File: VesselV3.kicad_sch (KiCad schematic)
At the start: 370 parts, among them IC1 USB3320C-EZK-TR, IC2 ORDiode(SWD/RST_SWITCH), J1 JTAG/SWD 10pins Headers, U1 LogicLevelShifter, Y1 25MHz

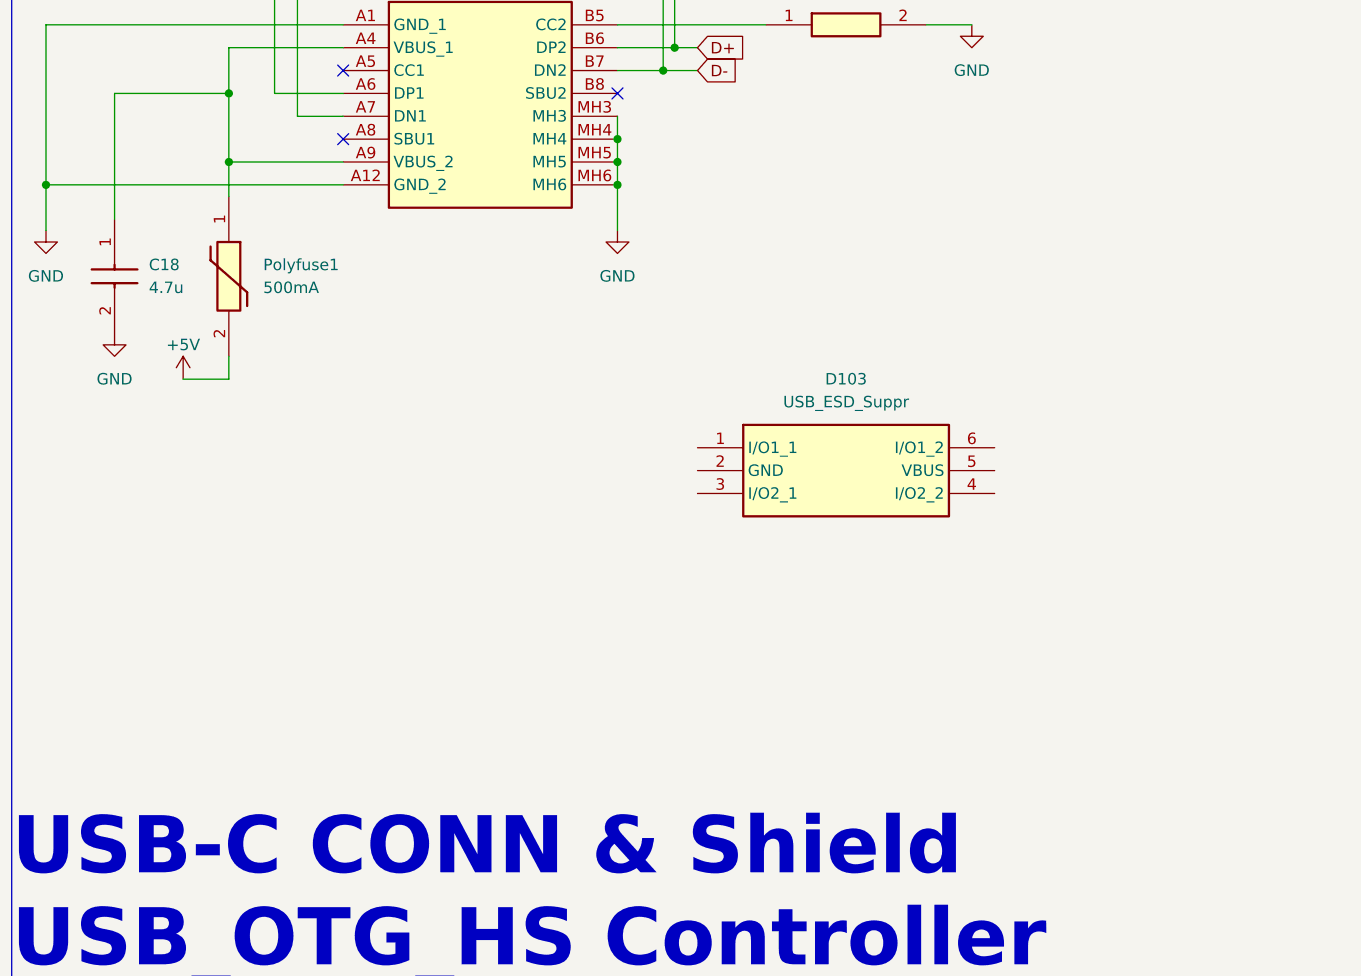
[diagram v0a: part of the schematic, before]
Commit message: ESD & Reverse Pol protections / + 5V regulator
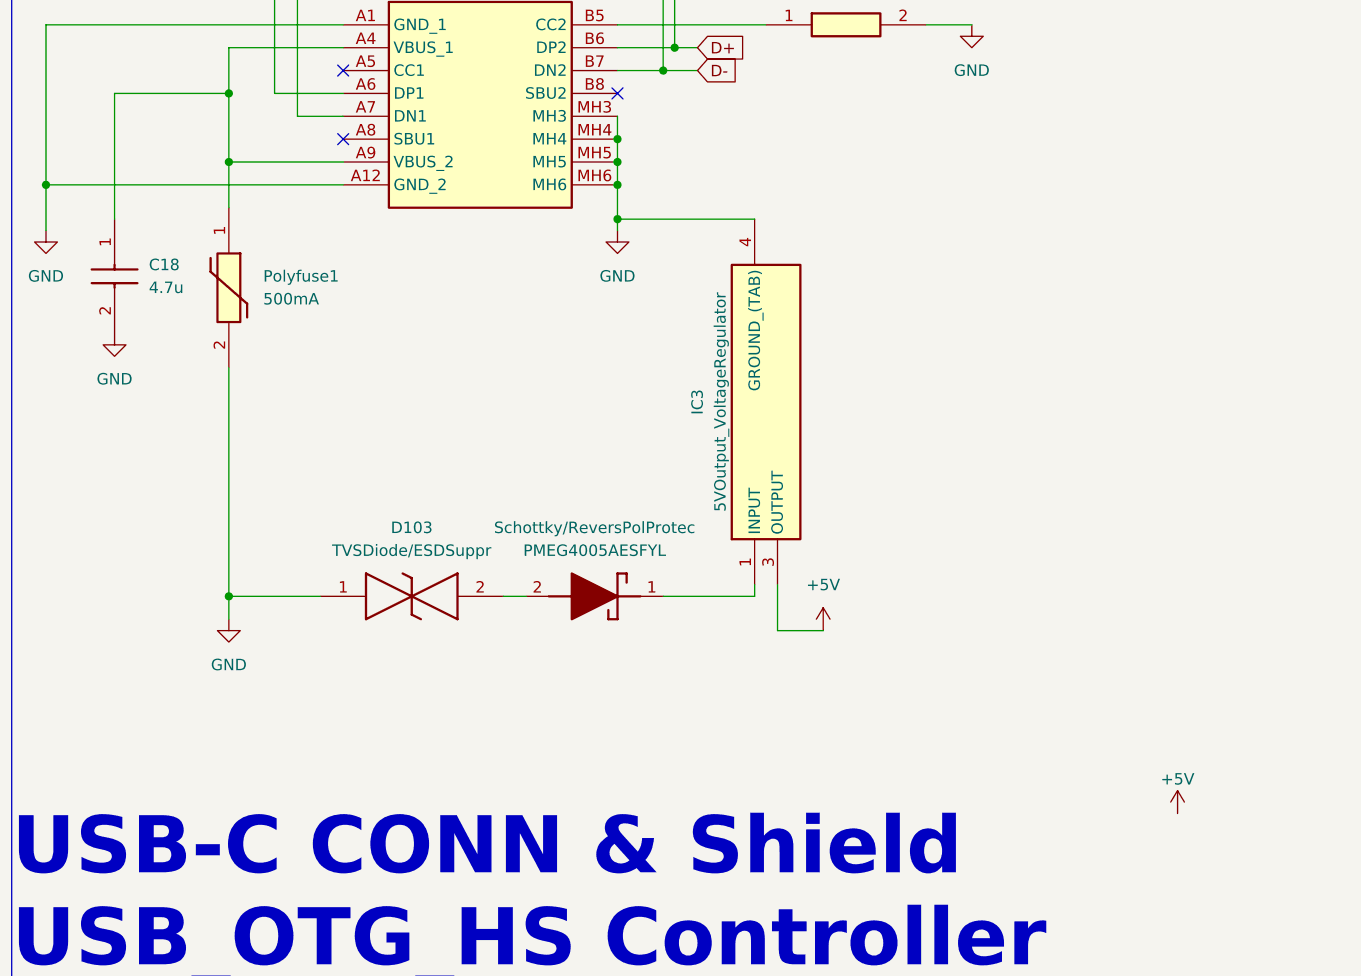
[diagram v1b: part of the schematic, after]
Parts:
- removed D103: USB_ESD_Suppr, SOT95P280X145-6N, symbol SamacSys_Parts:USBLC6-2SC6Y
- added D103: TVSDiode/ESDSuppr, SP433701WTG, symbol SamacSys_Parts:SP4337-01WTG
- added IC3: 5VOutput_VoltageRegulator, TO228P972X240-3N, symbol SamacSys_Parts:LF50ABDT-TR
- added Schottky/ReversPolProtec: PMEG4005AESFYL, PMEG4005AESFYL, symbol SamacSys_Parts:PMEG4005AESFYL
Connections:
- net +5V: now also IC3.3 (OUTPUT); no longer Polyfuse1.2
- net GND: now also Polyfuse1.2, D103.1, IC3.4 (GROUND_(TAB))
- new net: IC3.1 (INPUT), Schottky/ReversPolProtec.1 (K)
- new net: D103.2, Schottky/ReversPolProtec.2 (A)
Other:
- moved on the sheet: Polyfuse1

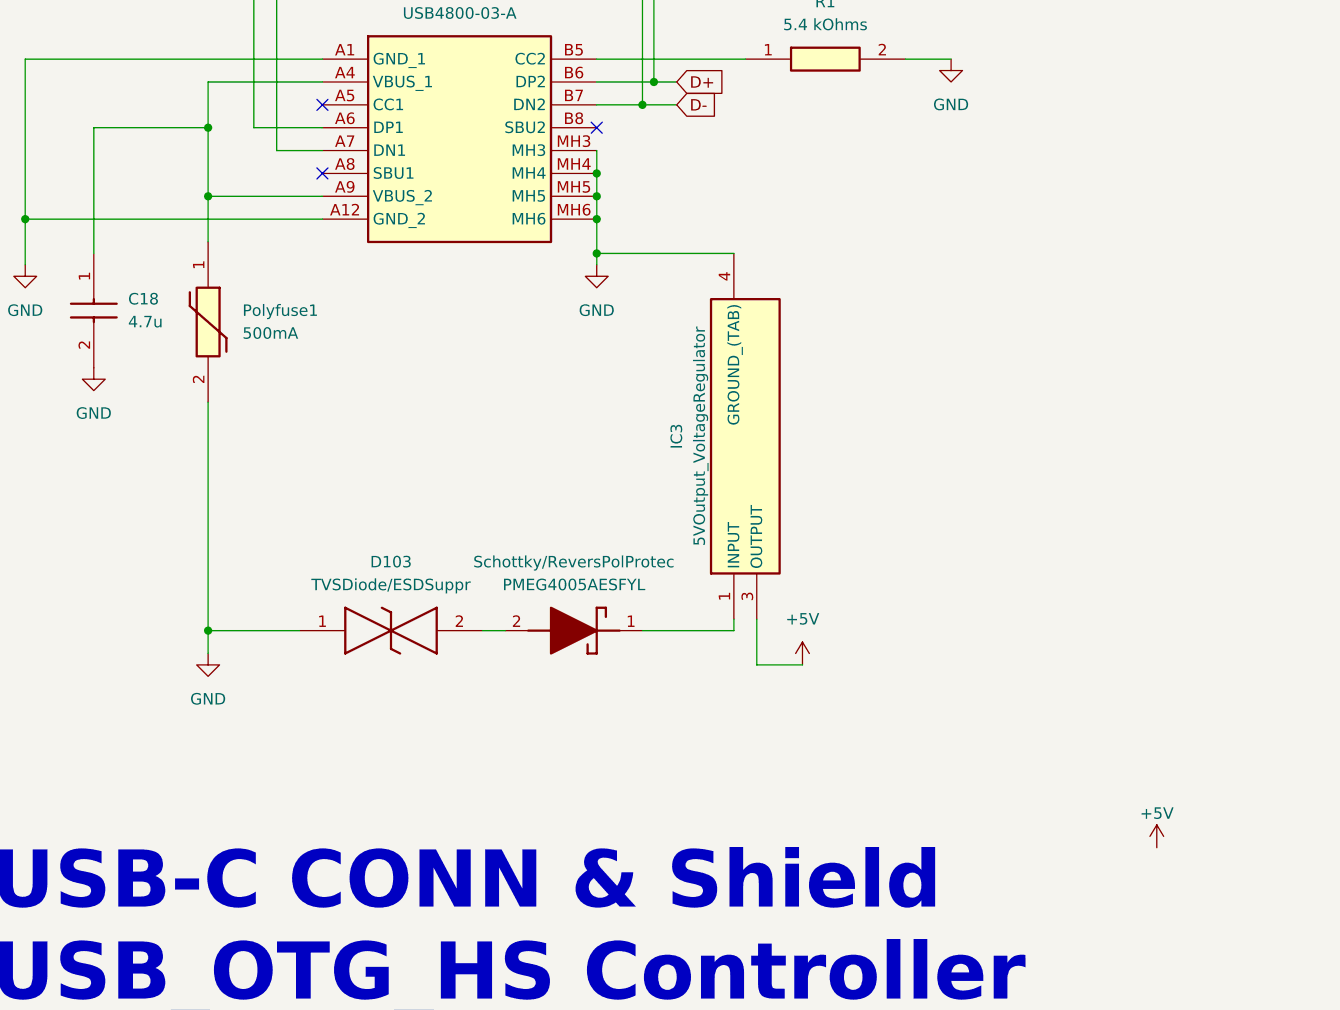
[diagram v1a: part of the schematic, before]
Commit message: Removed stray 5V, Added additional Caps
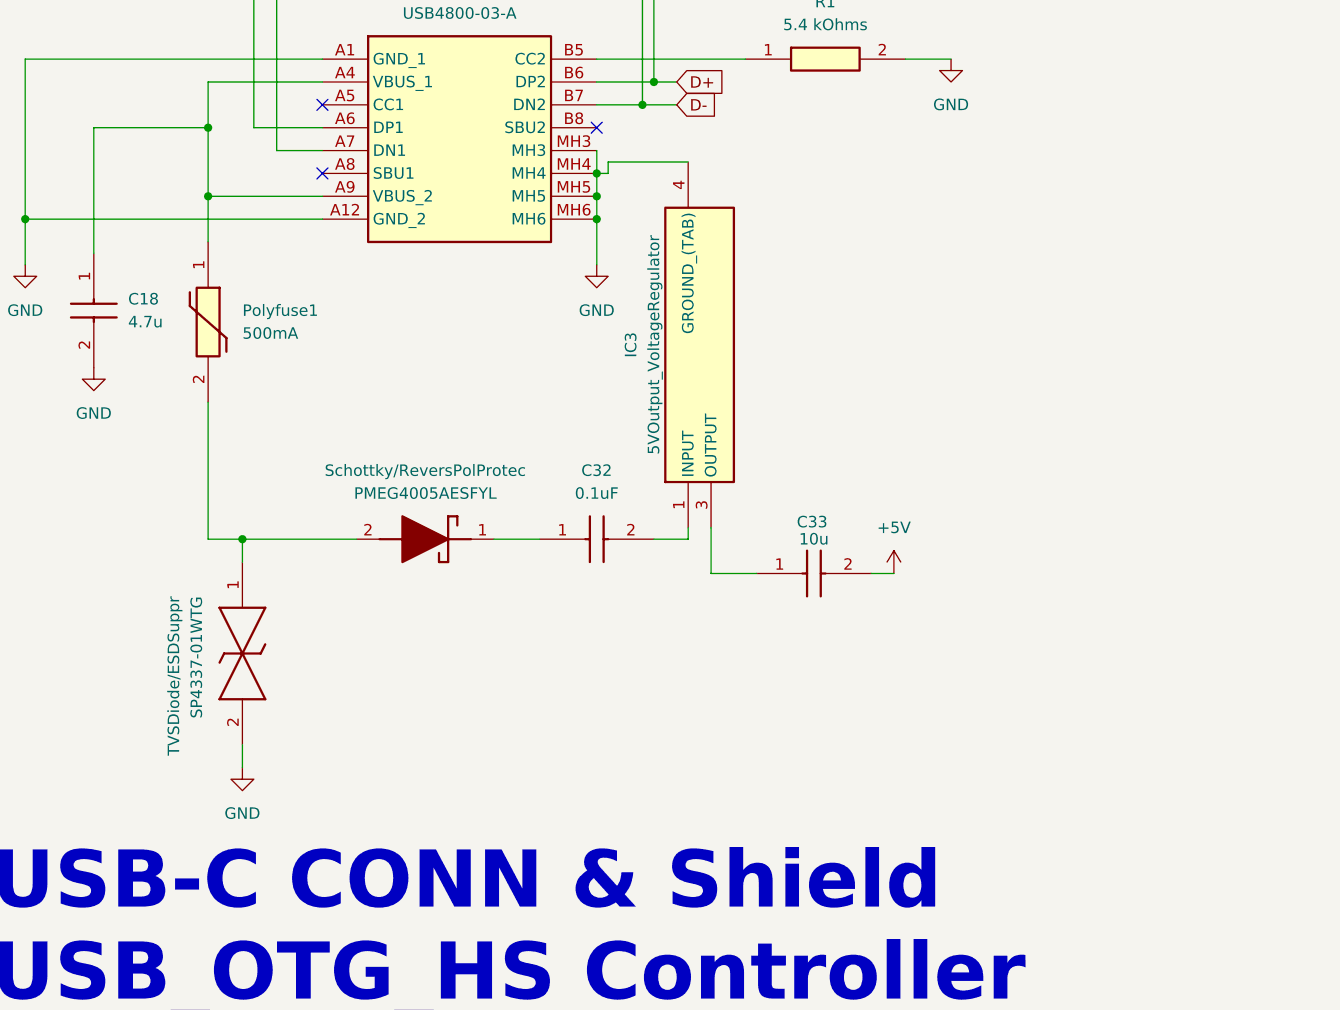
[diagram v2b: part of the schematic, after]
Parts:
- added C32: 0.1uF, SamacSys_Parts:CAPC1005X55N, symbol SamacSys_Parts:GRM155R71A104JA01D
- added C33: ${SIM.PARAMS}, SamacSys_Parts:CAPC2012X140N, symbol SamacSys_Parts:CL21A106KOQNNNE
- TVSDiode/ESDSuppr: renamed from D103; value TVSDiode/ESDSuppr -> SP4337-01WTG
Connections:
- net +5V: now also C33.2; no longer IC3.3 (OUTPUT)
- net GND: now also TVSDiode/ESDSuppr.2; no longer Polyfuse1.2, TVSDiode/ESDSuppr.1
- net at Schottky/ReversPolProtec.1 (K): now also C32.1; no longer IC3.1 (INPUT)
- net at Schottky/ReversPolProtec.2 (A): now also Polyfuse1.2, TVSDiode/ESDSuppr.1; no longer TVSDiode/ESDSuppr.2
- new net: C32.2, IC3.1 (INPUT)
- new net: C33.1, IC3.3 (OUTPUT)
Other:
- moved on the sheet: IC3, Schottky/ReversPolProtec, TVSDiode/ESDSuppr

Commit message: USB OTG D- & D+ fixes/Additional corrections
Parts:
- removed R12, R13: 4.7k, ERJ6ENF1000V, symbol SamacSys_Parts:ERJ-6ENF4701V
- removed R2, R3: ${SIM.PARAMS}, SamacSys_Parts:RESC2012X65N, symbol SamacSys_Parts:RMCF0805JT22R0
- removed R4: 1k, SamacSys_Parts:ERJ6ENF1000V, symbol SamacSys_Parts:ERJ-6ENF1001V
- removed S4: On/Off-DPDT, SamacSys_Parts:L201021MA04Q, symbol SamacSys_Parts:L201021MA04Q
- added R2: 10k, RESC2012X50N, symbol SamacSys_Parts:CRCW080510K0JNEC
- added S6: On/On SPDT, SPDTSlide:SW_L102021ML04Q, symbol SPDTSlide:L102021ML04Q
- added USB/ESD_Suppr1: USBLC6-2SC6Y, SOT95P280X145-6N, symbol SamacSys_Parts:USBLC6-2SC6Y
- C3: footprint C0805 -> SamacSys_Parts:C0805
- IC2: footprint SOTFL50P160X60-8N -> SamacSys_Parts:SOTFL50P160X60-8N
- IC3: footprint TO228P972X240-3N -> SamacSys_Parts:TO228P972X240-3N
- J1: footprint HUSSP10W40P127_2X5_635X340X420P -> SamacSys_Parts:HUSSP10W40P127_2X5_635X340X420P
- R11: footprint RESC2012X50N -> SamacSys_Parts:RESC2012X50N
- S5: footprint 450301014042 -> SamacSys_Parts:450301014042
- Schottky/ReversPolProtec1: renamed from Schottky/ReversPolProtec; footprint PMEG4005AESFYL -> SamacSys_Parts:PMEG4005AESFYL
- TVSDiode/ESDSuppr1: renamed from TVSDiode/ESDSuppr; footprint SP433701WTG -> SamacSys_Parts:SP433701WTG
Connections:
- net FMP_SCL is gone; now on net SCL: MCU1.37 (PC6)
- net FMP_SDA is gone; now on net SDA: MCU1.38 (PC7)
- net +5V: now also R2.2, S6.2, USB/ESD_Suppr1.5 (VBUS)
- net D+: now also USB/ESD_Suppr1.1 (I/O1_1)
- net D-: now also USB/ESD_Suppr1.3 (I/O2_1)
- net GND: now also USB/ESD_Suppr1.2 (GND)
- net On/OffSwitch: now also LED24.4 (VDD), LED7.4 (VDD), S6.1
- net ROW1: now also D19.1 (K)
- net at MX19.2: now also D19.2 (A)
- net at IC1.22 (VBUS): now also R2.1
- net DP: now reaches IC1.18 (DP)
- net DP: now also USB/ESD_Suppr1.6 (I/O1_2)
- net DM: now reaches IC1.19 (DM)
- net DM: now also USB/ESD_Suppr1.4 (I/O2_2)
- net SWO: no longer names the net of J1.6
- net VDD renamed +3.3V
- no-connect marks 24 -> 28
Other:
- moved on the sheet: C18, Polyfuse1, TVSDiode/ESDSuppr1

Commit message: Further fixes - Ibis models added
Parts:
- removed Inductor(3.9uH)1: ASPIAIG-F1040-3R9M-T, SamacSys_Parts:INDPM110100X400N, symbol SamacSys_Parts:ASPIAIG-F1040-3R9M-T
- removed R7: 80.6k, SamacSys_Parts:RESC2012X65N, symbol SamacSys_Parts:RMCF0805FT80K6
- added C34: 0.1uF, SamacSys_Parts:CAPC1005X55N, symbol SamacSys_Parts:GRM155R71A104JA01D
- added C35: 2.2uF, SamacSys_Parts:CAPC1608X90N, symbol SamacSys_Parts:CL10B225KP8NNNC
- added Inductor1: 3.9uH, Inductor3.9uH:IND_LQH32NH3R9J23L, symbol Inductor3.9uH:LQH32NH3R9J23L
- added R3: 80.6k, SamacSys_Parts:RESC2012X60N, symbol SamacSys_Parts:CR0805-FX-8062ELF
- added R7: 1k, RESC5025X65N, symbol SamacSys_Parts:CRS2010-FX-1001ELF
- C21: DigikeyPartNumber (none) -> 1276-2561-2-ND; Manufacturer_Part_Number (none) -> CL21C100CBANNNC; Mouser Part Number (none) -> 187-CL21C100CBANNNC
- MCU1: DigikeyPartNumber (none) -> 497-STM32F446RET6TR-ND
- R2: footprint RESC2012X50N -> SamacSys_Parts:RESC2012X50N
- USB/ESD_Suppr1: footprint SOT95P280X145-6N -> SamacSys_Parts:SOT95P280X145-6N
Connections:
- net +1V8: now also R3.1
- net +3.3V: now also Inductor1.2
- net +5V: now also C34.1, C35.1, R7.2
- net GND: now also BuckConverter1v8.6 (PG), R9.2, C34.2, C35.2
- net at BuckConverter1v8.5 (FB), C21.1, R8.1: now also R3.2
- net at BuckConverter3v3.5 (SW), C6.2: now also Inductor1.1
- net at C16.1, IC1.20 (VDD33): now also IC1.23 (ID)
- net at IC1.22 (VBUS), R2.1: now also R7.1
- no-connect marks 28 -> 26
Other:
- moved on the sheet: C16, C17, C24, C6, IC1, R2, R5, USB/ESD_Suppr1

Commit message: Rotary Enc 3V3 logic needs shifting to 5V (WIP)
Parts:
- added C36, C37: 0.01u, CAPC1005X56N, symbol SamacSys_Parts:0402ZC103JAT2A
- added R12, R13, R14, R4: 10k, SamacSys_Parts:RESC2012X50N, symbol SamacSys_Parts:CRCW080510K0JNEC
- added Rotary_Encoder(30mm): PEC12R-4230F-S0024, PEC12R4230FS0024, symbol SamacSys_Parts:PEC12R-4230F-S0024
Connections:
- net +3.3V: now also R14.1, R4.1
- net GND: now also MCU1.2 (PC13), C36.2, C37.2, Rotary_Encoder(30mm).1 (COM), Rotary_Encoder(30mm).2 (NO), Rotary_Encoder(30mm).C1 (COMMON)
- net ROTARY-ENC_A: now reaches MCU1.50 (PA15)
- net ROTARY-ENC_A: now also C37.1, R13.2
- net ROTARY-ENC_B: now reaches MCU1.55 (PB3)
- net ROTARY-ENC_B: now also C36.1, R12.2
- new net: R13.1, R14.2, Rotary_Encoder(30mm).A1 (CHANNEL_A)
- new net: R12.1, R4.2, Rotary_Encoder(30mm).B1 (CHANNEL_B)
- no-connect marks 26 -> 25
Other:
- moved on the sheet: C26

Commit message: Voltage Level Translator swapped - Rotary encoder fixed
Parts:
- removed C8: 0.1pF, Cap0.1SMD:CAP_600F-0805_ATC, symbol Cap0.1SMD:600F0R1AT250T
- removed U1: LogicLevelShifter, SN74AHCT125N - LogicLevelShifter:N14, symbol SN74AHCT125N - LogicLevelShifter:SN74AHCT125N
- added C38, C39: 0.1uF, SamacSys_Parts:CAPC1005X55N, symbol SamacSys_Parts:GRM155R71A104JA01D
- added IC4: BidirectionalLogicLevelShifter, SOP65P640X120-14N, symbol SamacSys_Parts:TXB0104PWR
- renumbered Rotary_Encoder(30mm) to Rotary_Encoder(30mm)1
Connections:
- net +3.3V: now also C38.1, IC4.1 (VCCA), IC4.8 (OE); no longer R14.1, R4.1
- net +5V: now also R14.1, R4.1, C39.1, IC4.14 (VCCB)
- net GND: now also C38.2, C39.2, IC4.7 (GND); no longer MCU1.2 (PC13), Rotary_Encoder(30mm)1.2 (NO)
- net LogicLevelShifterOutput: now also IC4.13 (B1)
- net RGBPIN: now also IC4.2 (A1)
- net ROTARY-ENC_A: now also IC4.12 (B2); no longer MCU1.50 (PA15)
- net ROTARY-ENC_B: now also IC4.11 (B3); no longer MCU1.55 (PB3)
- new net ROTARY-ENC_A_3v3: IC4.3 (A2), MCU1.50 (PA15)
- new net ROTARY-ENC_B_3v3: IC4.4 (A3), MCU1.55 (PB3)
- new net ROTARY-ENC_PUSH: IC4.10 (B4), Rotary_Encoder(30mm)1.2 (NO)
- new net ROTARY-ENC_PUSH_3v3: IC4.5 (A4), MCU1.2 (PC13)
- no-connect marks 25 -> 24
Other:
- note added: "LED Array (WS2812B 2020) Push Switch Rotary Encoder 4-Bit Bidirectional Voltage Level Translator"
- note removed: "LED Array (WS2812B 2020)"
- moved on the sheet: C36, C37, R12, R13, R14, R4, Rotary_Encoder(30mm)1, S6

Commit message: DFU compat, PNP Transistor, Pull-up resistors
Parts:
- removed IC2: ORDiode(SWD/RST_SWITCH), SamacSys_Parts:SOTFL50P160X60-8N, symbol SamacSys_Parts:LM66200DRLR
- removed S5: SPDT_ON/ON(ORDiode_LOW/HIGH), SamacSys_Parts:450301014042, symbol SamacSys_Parts:450301014042
- added C8: 0.1u, SamacSys_Parts:C0805, symbol SamacSys_Parts:C0805C104J8RACTU
- added IC6: AND Gate, SOT65P212X110-5N, symbol SamacSys_Parts:74AUP1G09GW-Q100H
- added PNPTransistor1: BC51-10PA-QX, BC55PASQX, symbol SamacSys_Parts:BC51-10PA-QX
- added R15: 5.4 kOhms, SamacSys_Parts:RESC1005X40N, symbol SamacSys_Parts:ESR01MZPF5101
- added R16, R17, R18, R19, R20: 10k, SamacSys_Parts:RESC2012X50N, symbol SamacSys_Parts:CRCW080510K0JNEC
- C36, C37: footprint CAPC1005X56N -> SamacSys_Parts:CAPC1005X56N
- IC4: footprint SOP65P640X120-14N -> SamacSys_Parts:SOP65P640X120-14N
- R7: footprint RESC5025X65N -> SamacSys_Parts:RESC5025X65N
- Rotary_Encoder(30mm)1: footprint PEC12R4230FS0024 -> SamacSys_Parts:PEC12R4230FS0024
- renumbered ResetSwitch1 to USB3320_ResetSwitch1
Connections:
- net RST_Switch is gone; now on net +3.3V: USB3320_ResetSwitch1.1
- net +3.3V: now also IC6.5 (VCC), PNPTransistor1.2 (E), R17.2, R18.1, R19.1, R20.1
- net GND: now also USB3320_ResetSwitch1.3, USB3320_ResetSwitch1.4, C8.2, IC6.3 (GND), R15.2, R16.2; no longer MCU1.60 (BOOT0), USB3320_ResetSwitch1.2
- net NRST: now also IC6.4 (Y), R17.1
- net RST: now also C8.1, IC6.1 (B), R18.2
- net GPIO_BOOT0_SIG: now reaches MCU1.56 (PB4)
- net GPIO_BOOT0_SIG: now also PNPTransistor1.1 (B)
- net at USB-C1.A5 (CC1): now also R15.1
- net USBResetGPIO-OUT renamed MCUResetGPIO-OUT
- net MCUResetGPIO-OUT: now also IC6.2 (A), R19.2; no longer IC1.27 (RESETB)
- new net BOOT0_PIN: MCU1.60 (BOOT0), PNPTransistor1.3 (C_1), PNPTransistor1.4 (C_2), R16.1
- new net USB3320_RST_Switch: IC1.27 (RESETB), R20.2, USB3320_ResetSwitch1.2
- no-connect marks 24 -> 19
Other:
- moved on the sheet: C26, C3, JSTPH4-PIN1, USB3320_ResetSwitch1

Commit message: Fixed LED GND/HSE Oscillator symbols
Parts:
- LED1, LED10, LED100, LED101, LED102, LED11, LED12, LED13, LED14, LED15, LED16, LED17, LED18, LED19, LED2, LED20, LED21, LED22, LED23, LED24, LED25, LED26, LED27, LED28, LED29, LED3, LED30, LED31, LED32, LED33, LED34, LED35, LED36, LED37, LED38, LED39, LED4, LED40, LED41, LED42, LED43, LED44, LED45, LED46, LED47, LED48, LED49, LED5, LED50, LED51, LED52, LED53, LED54, LED55, LED56, LED57, LED58, LED59, LED6, LED60, LED61, LED62, LED63, LED64, LED65, LED66, LED67, LED68, LED69, LED7, LED70, LED71, LED72, LED73, LED74, LED75, LED76, LED77, LED78, LED79, LED8, LED80, LED81, LED82, LED83, LED84, LED85, LED86, LED87, LED88, LED89, LED9, LED90, LED91, LED92, LED93, LED94, LED95, LED96, LED97, LED98, LED99: footprint WS2812BNano4684RGB-3rdParty:4684_ADA -> 4684_ADA
